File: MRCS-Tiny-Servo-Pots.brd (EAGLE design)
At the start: 100 x 80 mm, 11 parts, among them CON1 CONNECTOR-M03254-LOCK, U1 ATTINY85-20SH

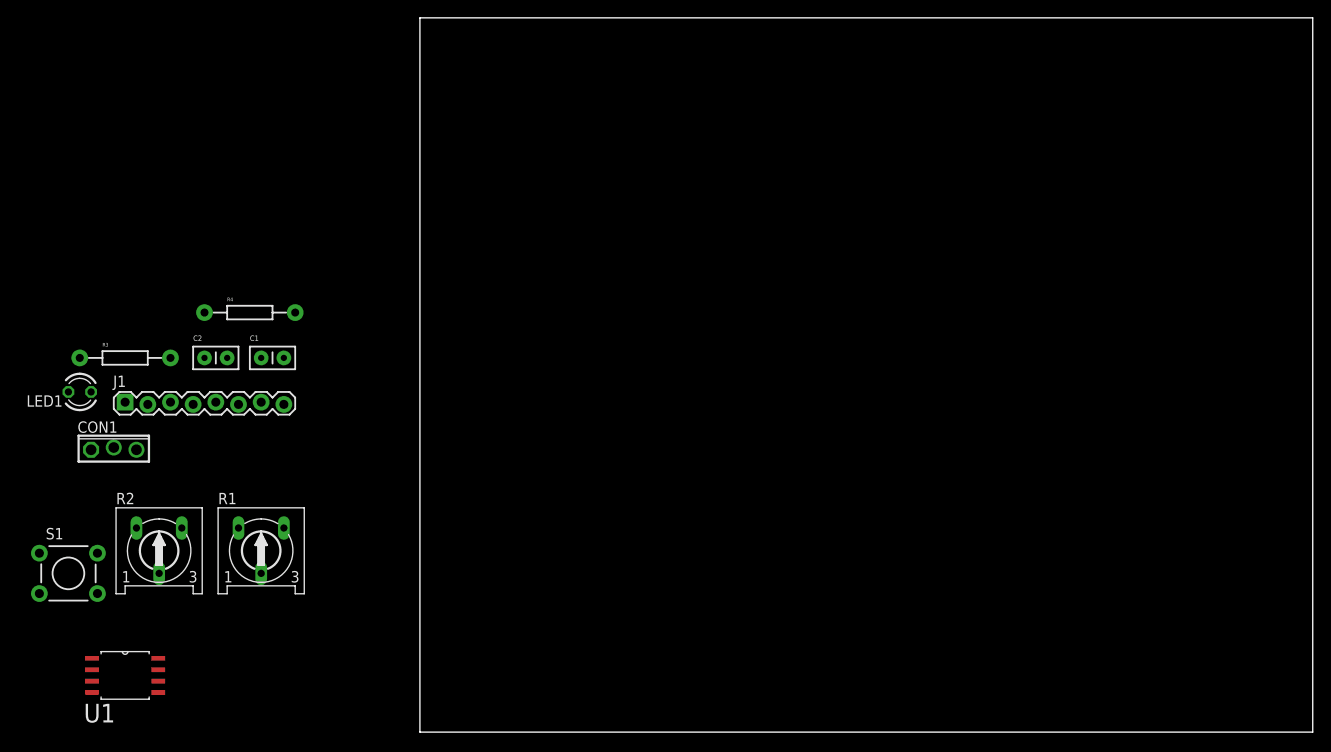
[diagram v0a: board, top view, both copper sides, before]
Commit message: first pass to production
this one is a little too big to go 2x3 so some changes will be made, also considering going surface mount, but only 2 resistors and a LED, the rest would be thru hole
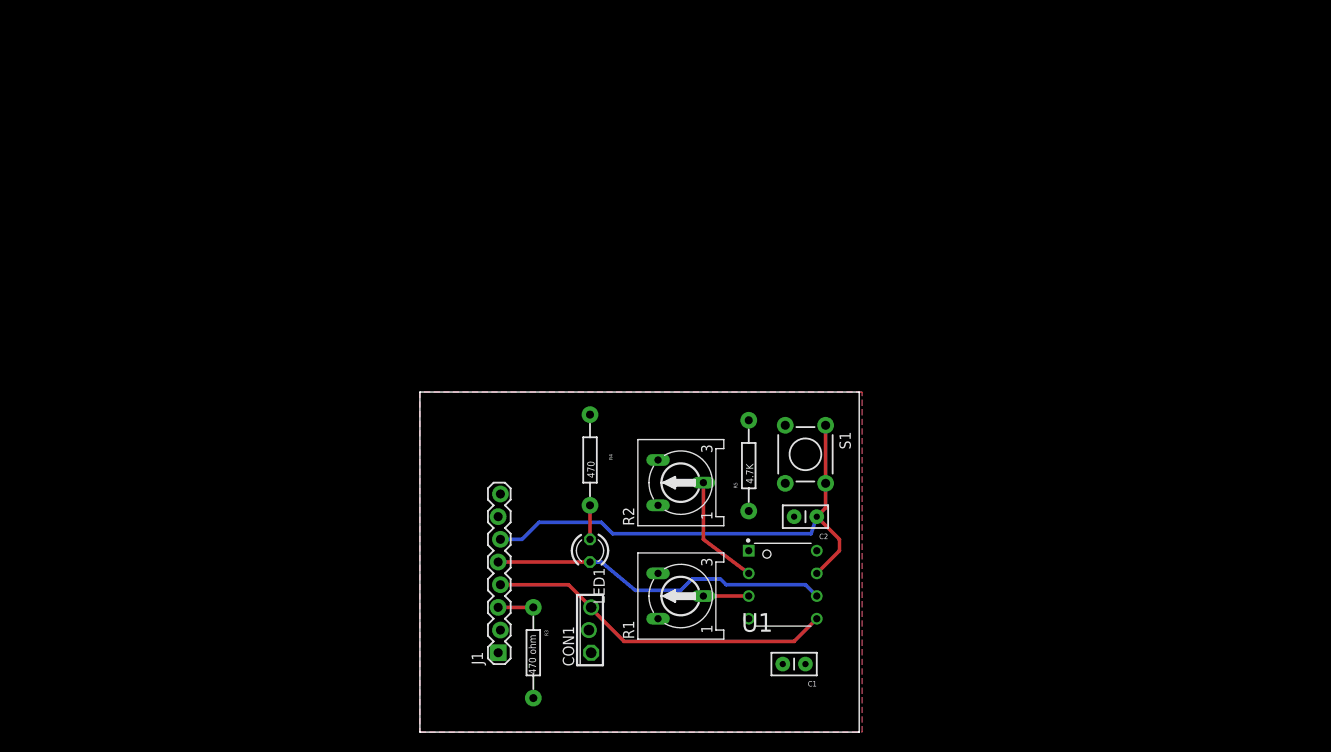
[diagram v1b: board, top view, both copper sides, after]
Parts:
- added R5: 4.7K, SPCoast:AXIAL-0.4-RES
- added U$1: (no value), MRCSLogoTop:MRCSLOGOTOP
- C1: value (none) -> .1 UF
- C2: value (none) -> 0.1 uF
- LED1: value (none) -> RED
- R1, R2: value (none) -> 10K
- R3: value (none) -> 470 ohm
- R4: value (none) -> 470
- U1: value ATTINY85-20SH -> ATTINY85-20PU; device ATTINY85-20SH:SOIC127P798X216-8N -> ATTINY85-20PU:DIP762W46P254L927H533Q8B
- moved S1 83.6 mm to (43.2, 31.1), turned to 270 degrees
- moved U1 74.4 mm to (40.6, 16.5)
- moved C2 68.4 mm to (43.2, 24.1), turned to 180 degrees
- moved C1 67.7 mm to (41.9, 7.62), turned to 180 degrees
- moved LED1 59.9 mm to (19.1, 20.3), turned to 90 degrees
- moved R2 58.9 mm to (29.2, 27.9), turned to 90 degrees
- moved CON1 57.1 mm to (19.1, 11.4), turned to 90 degrees
- moved R3 56.4 mm to (12.7, 8.89), turned to 270 degrees
- moved J1 50.4 mm to (8.89, 8.89), turned to 90 degrees
- moved R1 47.3 mm to (29.2, 15.2), turned to 90 degrees
- moved R4 41.5 mm to (19.1, 30.5), turned to 90 degrees
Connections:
- net ADC2 renamed ADC2-CCW
- net ADC3 renamed ADC3-CW
- removed net LED: J1.4, LED1.K, U1.5
- removed net SERVO: J1.5, U1.6
- new net LED1: J1.5, LED1.K, U1.6
- new net N$3: R5.P$1
- new net N$4: CON1.3, J1.4, U1.5
- new net VCC: U1.8
- net +5V: now also CON1.1, J1.7, R5.P$2; no longer U1.8
- net GND: now also C2.2, J1.8
- net INPUT: now also C2.1
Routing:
- net INPUT: track 0.00 -> 57.2 mm
- net N$4: track 0.00 -> 39.2 mm
- net LED1: track 0.00 -> 38.2 mm
- net ADC3-CW: track 0.00 -> 12.7 mm
- net ADC2-CCW: track 0.00 -> 5.08 mm
- net N$1: track 0.00 -> 3.94 mm
- net N$2: track 0.00 -> 3.81 mm
- added copper zone on layer 1, net +5V
- added copper zone on layer 16, net GND
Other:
- board size 100 x 80 mm -> 49.2 x 38.1 mm
- board text added: "GND +5 IN LED SER LP GND +5"
- board text added: "Seth Neumann 20220319"
- board text added: "Tiny85 Servo V1.0"
